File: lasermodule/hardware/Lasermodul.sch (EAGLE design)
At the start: 93 parts, among them IC1 MEGA8-AI

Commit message: lots of bugs fixed
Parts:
- 2A_4A: value PTC_FUSE -> PTC_FUSEPTC_FUSE_2920_UNIVERSAL; device wz:PTC_FUSE -> wz:PTC_FUSEPTC_FUSE_2920_UNIVERSAL
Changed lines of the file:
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@@
 <part name="AMP_IN_AGND" library="wz" deviceset="PIN-HEADER-1" device="PIN-HEADER-1"/>
 <part name="C13" library="wz" deviceset="C_EU" device="0603" value="100n"/>
-<part name="2A_4A" library="wz" deviceset="PTC_FUSE" device=""/>
+<part name="2A_4A" library="wz" deviceset="PTC_FUSE" device="PTC_FUSE_2920_UNIVERSAL"/>
 </parts>
 <sheets>

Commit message: lasermodul routing
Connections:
- net BACKLIGHT: now also ULN2803.O1; no longer ULN2803.O4
- net FLASHL_G: now also ULN2803.O3; no longer ULN2803.O2
- net FLASHL_R: now also ULN2803.O2; no longer ULN2803.O1
- net IR_CLK_-: now also ULN2803.O4; no longer ULN2803.O3
- net I_BACKLIGHT: now also ULN2803.I1; no longer ULN2803.I4
- net I_FLASHL_G: now also ULN2803.I3; no longer ULN2803.I2
- net I_FLASHL_R: now also ULN2803.I2; no longer ULN2803.I1
- net I_IR_CLK_-: now also ULN2803.I4; no longer ULN2803.I3
- net SCL_BUS: now also D2.C2; no longer D2.C3
- net SDA_BUS: now also D2.C3; no longer D2.C2

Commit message: routing
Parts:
- added H1, H2: MOUNT-PAD-ROUND3.0, holes:MOUNT-PAD-ROUND3.0
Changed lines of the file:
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@@
 <part name="C13" library="wz" deviceset="C_EU" device="0603" value="100n"/>
 <part name="2A_4A" library="wz" deviceset="PTC_FUSE" device="PTC_FUSE_2920_UNIVERSAL"/>
+<part name="H1" library="holes" deviceset="MOUNT-PAD-ROUND" device="3.0"/>
+<part name="H2" library="holes" deviceset="MOUNT-PAD-ROUND" device="3.0"/>
 </parts>
 <sheets>
@@
 <instance part="C13" gate="G$1" x="-30.48" y="17.78" rot="R90"/>
 <instance part="2A_4A" gate="G$1" x="-106.68" y="-83.82"/>
+<instance part="H1" gate="G$1" x="22.86" y="63.5"/>
+<instance part="H2" gate="G$1" x="5.08" y="63.5"/>
 </instances>
 <busses>

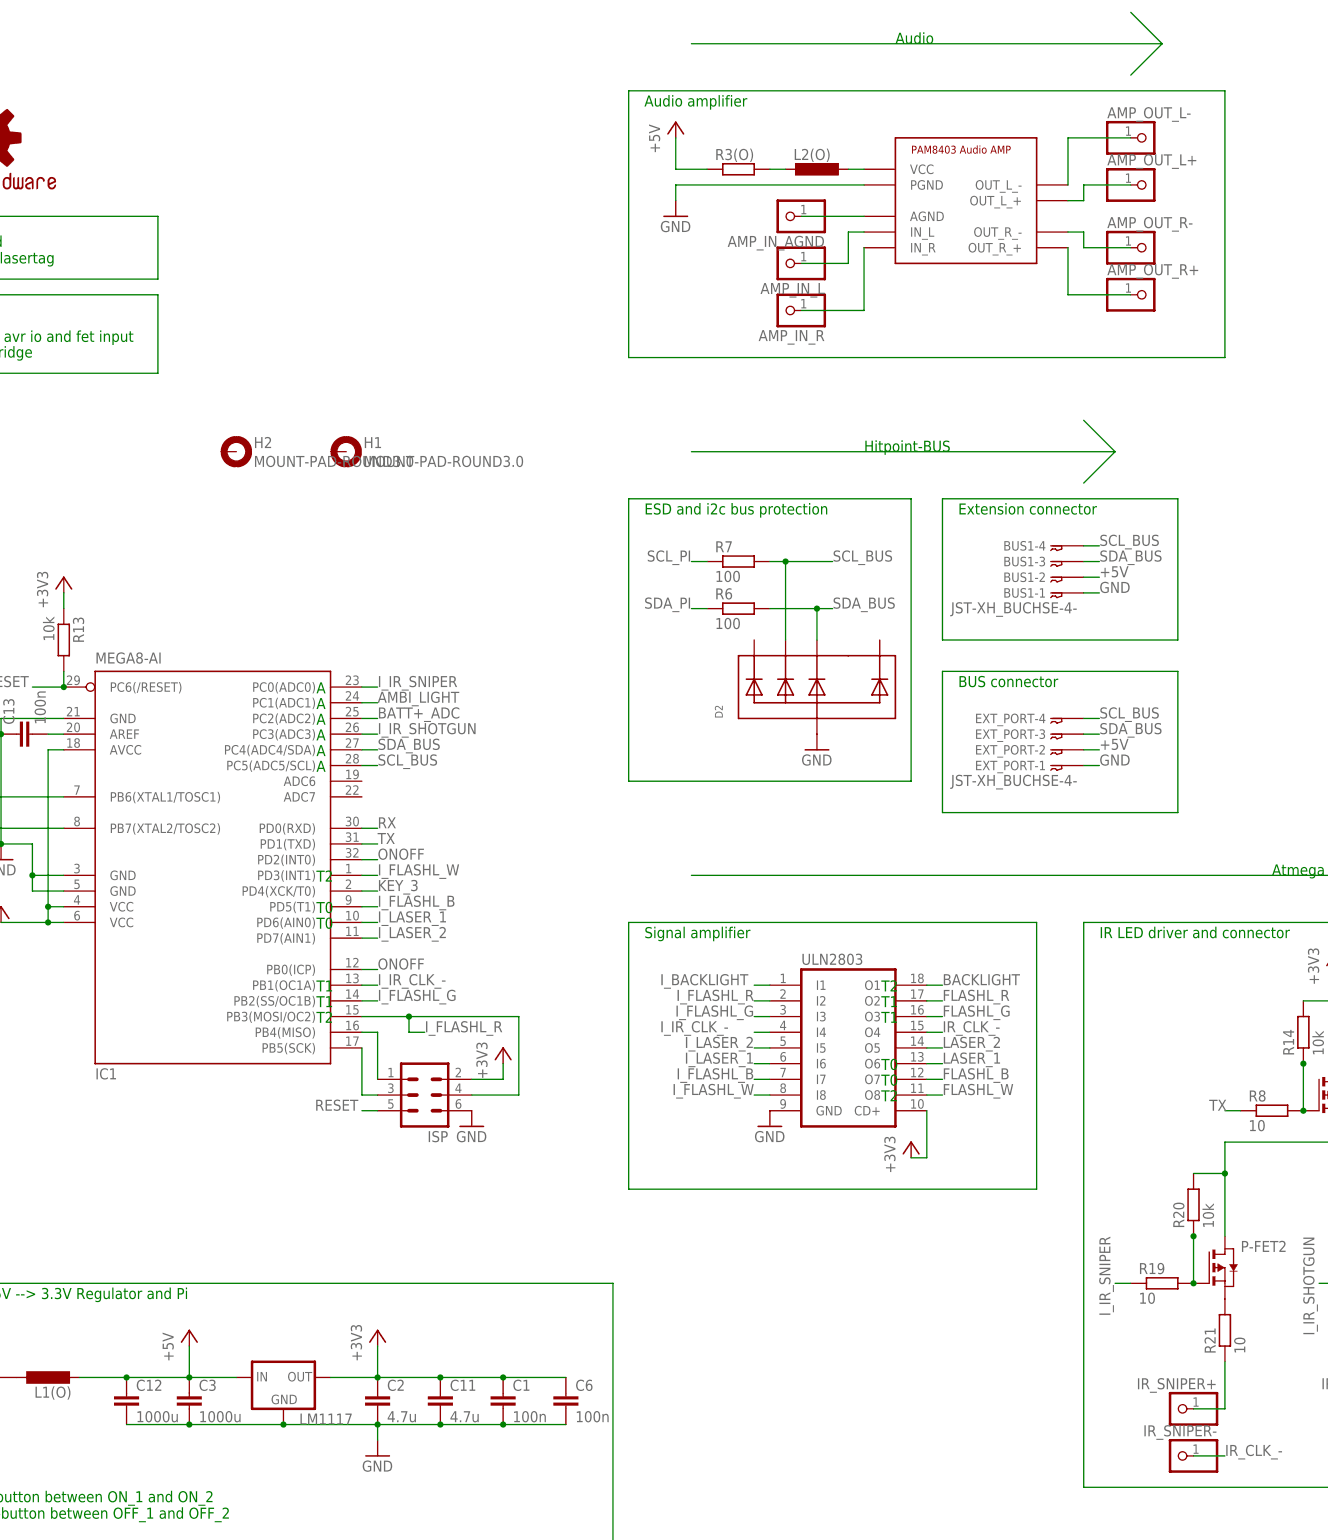
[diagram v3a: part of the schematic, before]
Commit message: routing and a bit case design
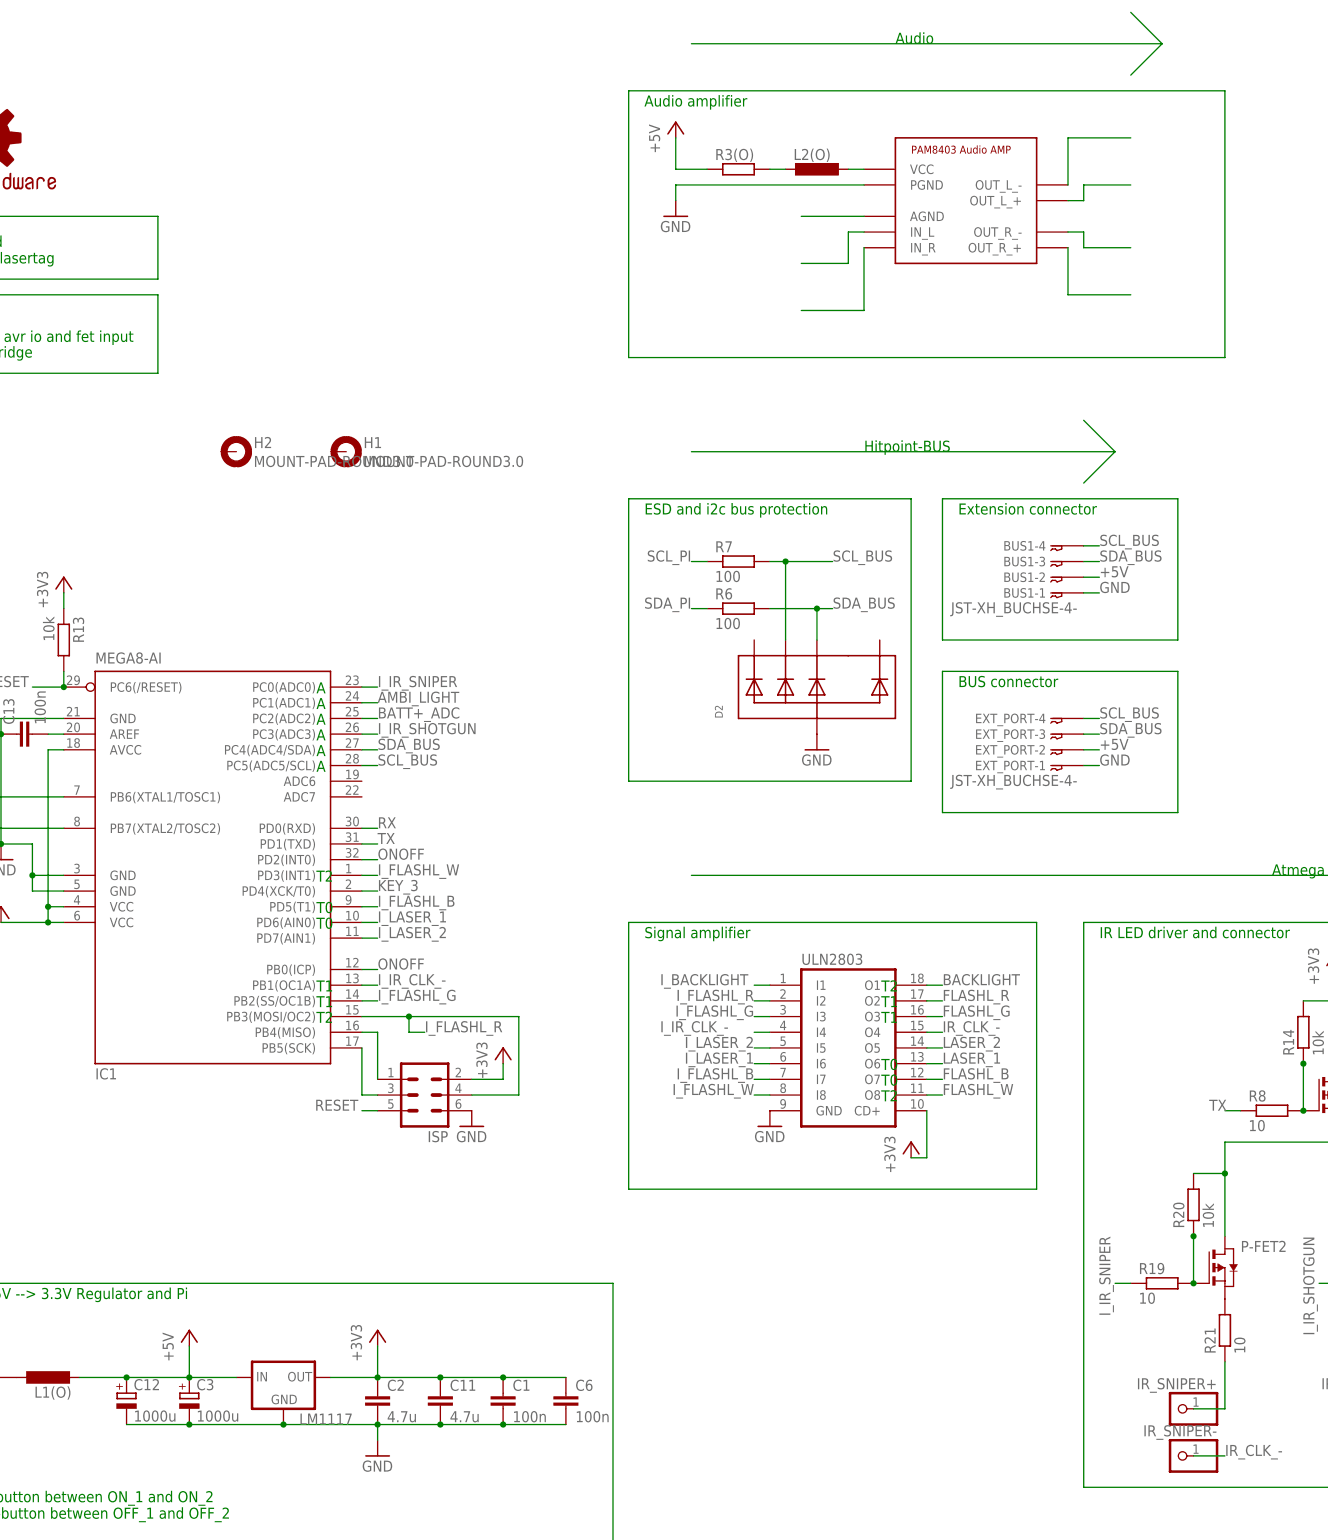
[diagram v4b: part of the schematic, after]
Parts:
- removed AMP_IN_AGND, AMP_IN_L, AMP_IN_R, AMP_OUT_L+, AMP_OUT_L-, AMP_OUT_R+, AMP_OUT_R-: (no value), wz:PIN-HEADER-1PIN-HEADER-1
- C12, C3: device wz:C_EUCAP_UNIVERSAL -> wz:C_EU_POLCAP_UNIVERSAL
- KEY1, KEY1G, KEY2, KEY2G, KEY3, KEY3G: device wz:PIN-HEADER-1PIN-HEADER-1 -> wz:PIN-HEADER-1PIN-HEADER-1_SMALL
- LOGO1: device wz:OSHW-LOGOM -> SparkFun-Aesthetics:OSHW-LOGOM
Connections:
- net +5V: now also C12.+, C3.+; no longer C12.1, C3.1
- net AMP_IN_AGND: no longer AMP_IN_AGND.1
- net AMP_IN_L: no longer AMP_IN_L.1
- net AMP_IN_R: no longer AMP_IN_R.1
- net AMP_OUT_L+: no longer AMP_OUT_L+.1
- net AMP_OUT_L-: no longer AMP_OUT_L-.1
- net AMP_OUT_R+: no longer AMP_OUT_R+.1
- net AMP_OUT_R-: no longer AMP_OUT_R-.1
- net GND: now also C12.-, C3.-; no longer C12.2, C3.2

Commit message: routing
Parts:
- added SJ1: (no value), jumper:SJ
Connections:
- net AMP_IN_AGND: now also SJ1.2
- net GND: now also SJ1.1
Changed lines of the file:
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@@
 <grid distance="0.1" unitdist="inch" unit="inch" style="lines" multiple="1" display="no" altdistance="0.01" altunitdist="inch" altunit="inch"/>
 <layers>
-<layer number="1" name="Top" color="4" fill="1" visible="yes" active="no"/>
-<layer number="16" name="Bottom" color="1" fill="1" visible="yes" active="no"/>
-<layer number="17" name="Pads" color="2" fill="1" visible="yes" active="no"/>
-<layer number="18" name="Vias" color="2" fill="1" visible="yes" active="no"/>
-<layer number="19" name="Unrouted" color="6" fill="1" visible="yes" active="no"/>
-<layer number="20" name="Dimension" color="15" fill="1" visible="yes" active="no"/>
-<layer number="21" name="tPlace" color="7" fill="1" visible="yes" active="no"/>
-<layer number="22" name="bPlace" color="7" fill="1" visible="yes" active="no"/>
-<layer number="23" name="tOrigins" color="15" fill="1" visible="yes" active="no"/>
-<layer number="24" name="bOrigins" color="15" fill="1" visible="yes" active="no"/>
-<layer number="25" name="tNames" color="7" fill="1" visible="yes" active="no"/>
-<layer number="26" name="bNames" color="7" fill="1" visible="yes" active="no"/>
-<layer number="27" name="tValues" color="7" fill="1" visible="yes" active="no"/>
-<layer number="28" name="bValues" color="7" fill="1" visible="yes" active="no"/>
+<layer number="1" name="Top" color="4" fill="1" visible="no" active="no"/>
+<layer number="16" name="Bottom" color="1" fill="1" visible="no" active="no"/>
+<layer number="17" name="Pads" color="2" fill="1" visible="no" active="no"/>
+<layer number="18" name="Vias" color="2" fill="1" visible="no" active="no"/>
+<layer number="19" name="Unrouted" color="6" fill="1" visible="no" active="no"/>
+<layer number="20" name="Dimension" color="15" fill="1" visible="no" active="no"/>
+<layer number="21" name="tPlace" color="7" fill="1" visible="no" active="no"/>
+<layer number="22" name="bPlace" color="7" fill="1" visible="no" active="no"/>
+<layer number="23" name="tOrigins" color="15" fill="1" visible="no" active="no"/>
+<layer number="24" name="bOrigins" color="15" fill="1" visible="no" active="no"/>
+<layer number="25" name="tNames" color="7" fill="1" visible="no" active="no"/>
+<layer number="26" name="bNames" color="7" fill="1" visible="no" active="no"/>
+<layer number="27" name="tValues" color="7" fill="1" visible="no" active="no"/>
+<layer number="28" name="bValues" color="7" fill="1" visible="no" active="no"/>
 <layer number="29" name="tStop" color="7" fill="3" visible="no" active="no"/>
 <layer number="30" name="bStop" color="7" fill="6" visible="no" active="no"/>
@@
 <layer number="35" name="tGlue" color="7" fill="4" visible="no" active="no"/>
 <layer number="36" name="bGlue" color="7" fill="5" visible="no" active="no"/>
-<layer number="37" name="tTest" color="7" fill="1" visible="yes" active="no"/>
-<layer number="38" name="bTest" color="7" fill="1" visible="yes" active="no"/>
+<layer number="37" name="tTest" color="7" fill="1" visible="no" active="no"/>
+<layer number="38" name="bTest" color="7" fill="1" visible="no" active="no"/>
 <layer number="39" name="tKeepout" color="4" fill="11" visible="no" active="no"/>
 <layer number="40" name="bKeepout" color="1" fill="11" visible="no" active="no"/>
@@
 <layer number="44" name="Drills" color="7" fill="1" visible="no" active="no"/>
 <layer number="45" name="Holes" color="7" fill="1" visible="no" active="no"/>
-<layer number="46" name="Milling" color="3" fill="1" visible="yes" active="no"/>
-<layer number="47" name="Measures" color="7" fill="1" visible="yes" active="no"/>
-<layer number="48" name="Document" color="7" fill="1" visible="yes" active="no"/>
-<layer number="49" name="Reference" color="7" fill="1" visible="yes" active="no"/>
-<layer number="50" name="dxf" color="7" fill="1" visible="yes" active="no"/>
-<layer number="51" name="tDocu" color="7" fill="1" visible="yes" active="no"/>
-<layer number="52" name="bDocu" color="7" fill="1" visible="yes" active="no"/>
-<layer number="53" name="tGND_GNDA" color="7" fill="9" visible="yes" active="no"/>
-<layer number="54" name="bGND_GNDA" color="1" fill="9" visible="yes" active="no"/>
-<layer number="56" name="wert" color="7" fill="1" visible="yes" active="no"/>
-<layer number="57" name="tCAD" color="7" fill="1" visible="yes" active="no"/>
-<layer number="59" name="tCarbon" color="7" fill="1" visible="yes" active="no"/>
-<layer number="60" name="bCarbon" color="7" fill="1" visible="yes" active="no"/>
+<layer number="46" name="Milling" color="3" fill="1" visible="no" active="no"/>
+<layer number="47" name="Measures" color="7" fill="1" visible="no" active="no"/>
+<layer number="48" name="Document" color="7" fill="1" visible="no" active="no"/>
+<layer number="49" name="Reference" color="7" fill="1" visible="no" active="no"/>
+<layer number="50" name="dxf" color="7" fill="1" visible="no" active="no"/>
+<layer number="51" name="tDocu" color="7" fill="1" visible="no" active="no"/>
+<layer number="52" name="bDocu" color="7" fill="1" visible="no" active="no"/>
+<layer number="53" name="tGND_GNDA" color="7" fill="9" visible="no" active="no"/>
+<layer number="54" name="bGND_GNDA" color="1" fill="9" visible="no" active="no"/>
+<layer number="56" name="wert" color="7" fill="1" visible="no" active="no"/>
+<layer number="57" name="tCAD" color="7" fill="1" visible="no" active="no"/>
+<layer number="59" name="tCarbon" color="7" fill="1" visible="no" active="no"/>
+<layer number="60" name="bCarbon" color="7" fill="1" visible="no" active="no"/>
 <layer number="90" name="Modules" color="5" fill="1" visible="yes" active="yes"/>
 <layer number="91" name="Nets" color="2" fill="1" visible="yes" active="yes"/>
@@
 <part name="H2" library="holes" deviceset="MOUNT-PAD-ROUND" device="3.0"/>
 <part name="LOGO1" library="SparkFun-Aesthetics" deviceset="OSHW-LOGO" device="M"/>
+<part name="SJ1" library="jumper" deviceset="SJ" device=""/>
 </parts>
 <sheets>
@@
 <instance part="P+3" gate="1" x="76.2" y="116.84"/>
 <instance part="U$4" gate="G$1" x="121.92" y="101.6"/>
-<instance part="GND15" gate="1" x="76.2" y="101.6"/>
+<instance part="GND15" gate="1" x="76.2" y="96.52"/>
 <instance part="DISPLAY" gate="1" x="248.92" y="121.92" rot="R270"/>
 <instance part="LDR_2" gate="G$1" x="-96.52" y="22.86"/>
@@
 <instance part="H2" gate="G$1" x="5.08" y="63.5"/>
 <instance part="LOGO1" gate="G$1" x="-35.56" y="114.3"/>
+<instance part="SJ1" gate="1" x="91.44" y="101.6"/>
 </instances>
 <busses>
@@
 <wire x1="106.68" y1="106.68" x2="76.2" y2="106.68" width="0.1524" layer="91"/>
 <pinref part="GND15" gate="1" pin="GND"/>
-<wire x1="76.2" y1="106.68" x2="76.2" y2="104.14" width="0.1524" layer="91"/>
+<wire x1="76.2" y1="106.68" x2="76.2" y2="101.6" width="0.1524" layer="91"/>
+<pinref part="SJ1" gate="1" pin="1"/>
+<wire x1="76.2" y1="101.6" x2="76.2" y2="99.06" width="0.1524" layer="91"/>
+<wire x1="86.36" y1="101.6" x2="76.2" y2="101.6" width="0.1524" layer="91"/>
+<junction x="76.2" y="101.6"/>
 </segment>
 <segment>
@@
 <pinref part="U$4" gate="G$1" pin="AGND"/>
 <wire x1="96.52" y1="101.6" x2="106.68" y2="101.6" width="0.1524" layer="91"/>
-</segment>
-</net>
+<pinref part="SJ1" gate="1" pin="2"/>
+</segment>
+</net>

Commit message: routing
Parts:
- removed KEY1, KEY1G, KEY2, KEY2G, KEY3, KEY3G: (no value), wz:PIN-HEADER-1PIN-HEADER-1_SMALL
- removed R2(O): (no value), wz:R_EU0603_CLOSED
- removed SJ1: (no value), jumper:SJ
- added BUTTONS: (no value), wz:PIN-HEADER-3X2
- added C14: 4.7u, wz:C_EU0805
- added L1: (no value), rcl:L-EUL2825P
- added R20(O): (no value), wz:R_EU0603_CLOSED
- added U$5, U$6: FIDUCIAL, adafruit:FIDUCIAL
- C1: value 100n -> 1000u; device wz:C_EU0603 -> wz:C_EU_POL
- C11: value 4.7u -> 100n; device wz:C_EU0805 -> wz:C_EU0603
- C12: value 1000u -> 100n; device wz:C_EU_POLCAP_UNIVERSAL -> wz:C_EU0603
- C2: value 4.7u -> 1000u; device wz:C_EU0805 -> wz:C_EU_POL
- C3: value 1000u -> 4.7u; device wz:C_EU_POLCAP_UNIVERSAL -> wz:C_EU0805
- C4: value 100n -> 4.7u; device wz:C_EU0603 -> wz:C_EU0805
- ISP: device con-lstb:MA03-2 -> wz:PIN-HEADER-3X2
- PI: device con-lstb:MA20-2 -> wz:PIN-HEADER-20X2
- renumbered FLASHL_5V to FRONTLED_5V, FLASHL_B to FRONTLED_B, FLASHL_G to FRONTLED_G, FLASHL_R to FRONTLED_R, FLASHL_W to FRONTLED_W, IR_SHOTGUN+ to IR_SHOTG+, IR_SHOTGUN- to IR_SHOTG-, L1(O) to L_PWR(O), L2(O) to L_AMP(O), R19 to R1, R20 to R2
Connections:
- removed net AMP_IN_AGND: SJ1.2, U$4.AGND
- removed net AMP_IN_L: U$4.IN_L
- removed net AMP_IN_R: U$4.IN_R
- removed net AMP_OUT_L+: U$4.OUT_L_+
- removed net AMP_OUT_L-: U$4.OUT_L_-
- removed net AMP_OUT_R+: U$4.OUT_R_+
- removed net AMP_OUT_R-: U$4.OUT_R_-
- removed net KEY_1: IC1.PB7(XTAL2/TOSC2), KEY1.1
- removed net KEY_2: IC1.PB6(XTAL1/TOSC1), KEY2.1
- removed net KEY_3: IC1.PD4(XCK/T0), KEY3.1
- new net BUTTON_1: BUTTONS.2, IC1.PB7(XTAL2/TOSC2)
- new net BUTTON_2: BUTTONS.4, IC1.PB6(XTAL1/TOSC1)
- new net BUTTON_3: BUTTONS.6, IC1.PD4(XCK/T0)
- new net N$5: L1.2, U$4.AGND
- net +3V3: now also C3.1, C4.1, C5.1; no longer C1.1, C11.1, C2.1
- net +5V: now also C1.+, C14.1, C2.+; no longer C12.+, C3.+
- net AMBI_LIGHT: now also C11.1; no longer C4.1
- net BATT+_ADC: now also C12.1; no longer C5.1
- net GND: now also BUTTONS.1, BUTTONS.3, BUTTONS.5, C1.-, C12.2, C14.2, C2.-, C3.2, L1.1; no longer C1.2, C12.-, C2.2, C3.-, KEY1G.1, KEY2G.1, KEY3G.1, SJ1.1
- net LASER_2: now also R20(O).1; no longer R2(O).1
- net LASER_2-: now also R20(O).2; no longer R2(O).2
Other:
- moved on the sheet: C11, C4, C5, C6, LASER_1+, LASER_1-, LASER_2+, LASER_2-, LM1117, R1(O)
